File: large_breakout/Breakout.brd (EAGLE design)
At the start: 30.7 x 49.7 mm, 17 parts, among them X1 RJ45-8X, X2 4TERM, X3 3TERM, X4 3TERM, X5 3TERM

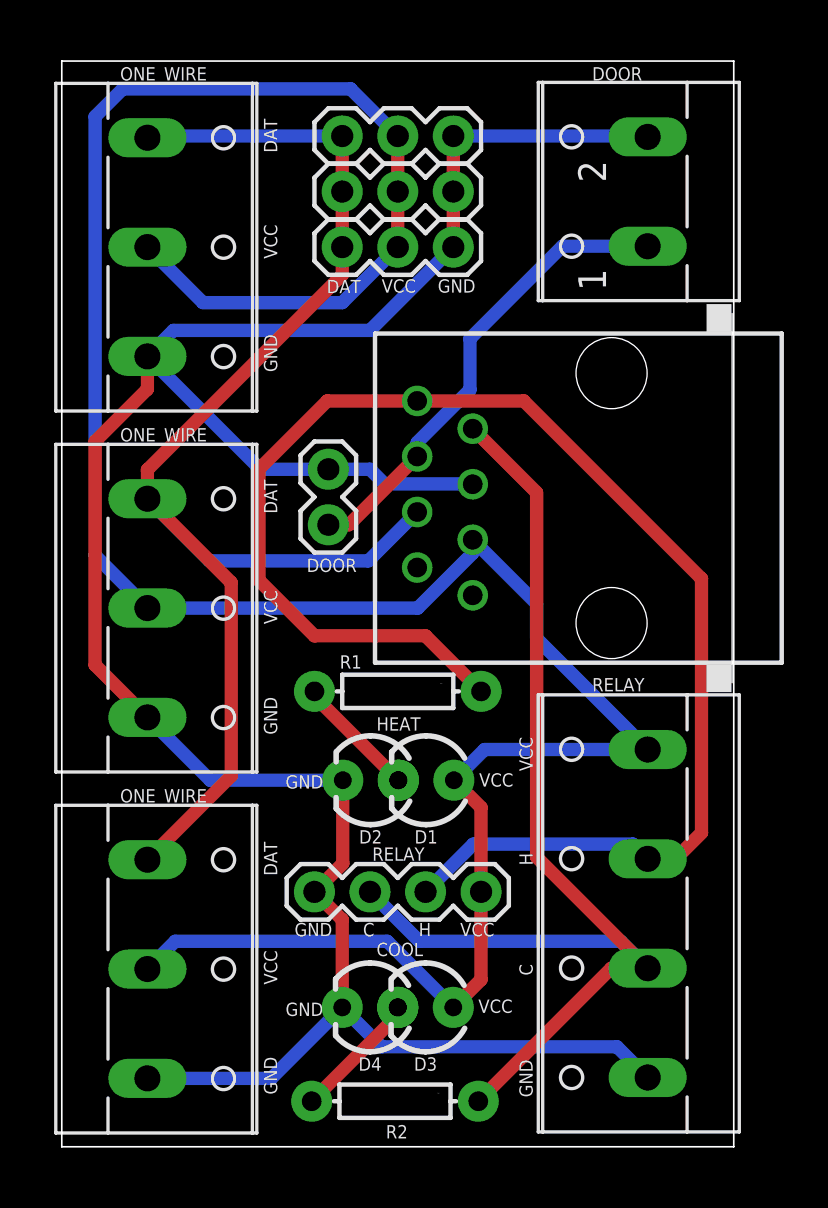
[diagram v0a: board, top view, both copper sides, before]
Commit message: Remove a bunch of 90's
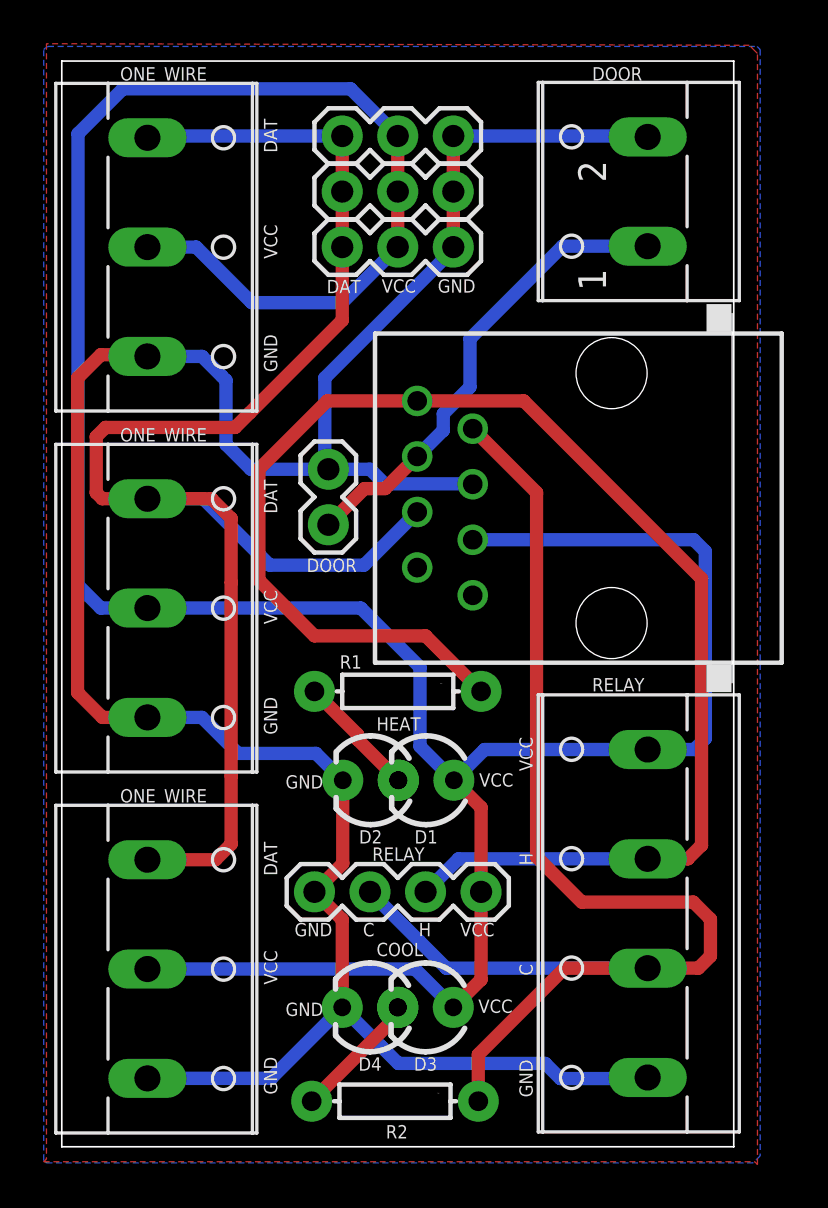
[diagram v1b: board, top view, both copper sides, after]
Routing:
- net VCC: track 123.5 -> 136.5 mm
- net DATA: track 63.3 -> 73.7 mm
- net COOL: track 52.4 -> 60.4 mm
- net GND: track 113.0 -> 114.6 mm
- added copper zone on layer 16, net GND
- added copper zone on layer 1, net VCC
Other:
- board text added: "5 - GND 6 - DOOR 7 - COOL 8 - HEAT"
- board text added: "RJ45 Pinout: 1 - 2 - 3 - VCC 4 - DATA"
- board text removed: "RJ45 Pinout: 1 - 5 - GND 2 - 6 - DOOR 3 - VCC 7 - COOL 4 - DATA 8 - HEAT"
